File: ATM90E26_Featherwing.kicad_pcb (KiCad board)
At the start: 2 copper layers, 49.9 x 39.4 mm, 59 parts, among them J1 ST-PJ-312, J2 4P-SMD-2.0-90D, J3 4P-SMD-2.0-90D, J4 12V AC, Q1 8.192MHz, U1 ATM90E26, U2 CJT1117-5.0-SOT223

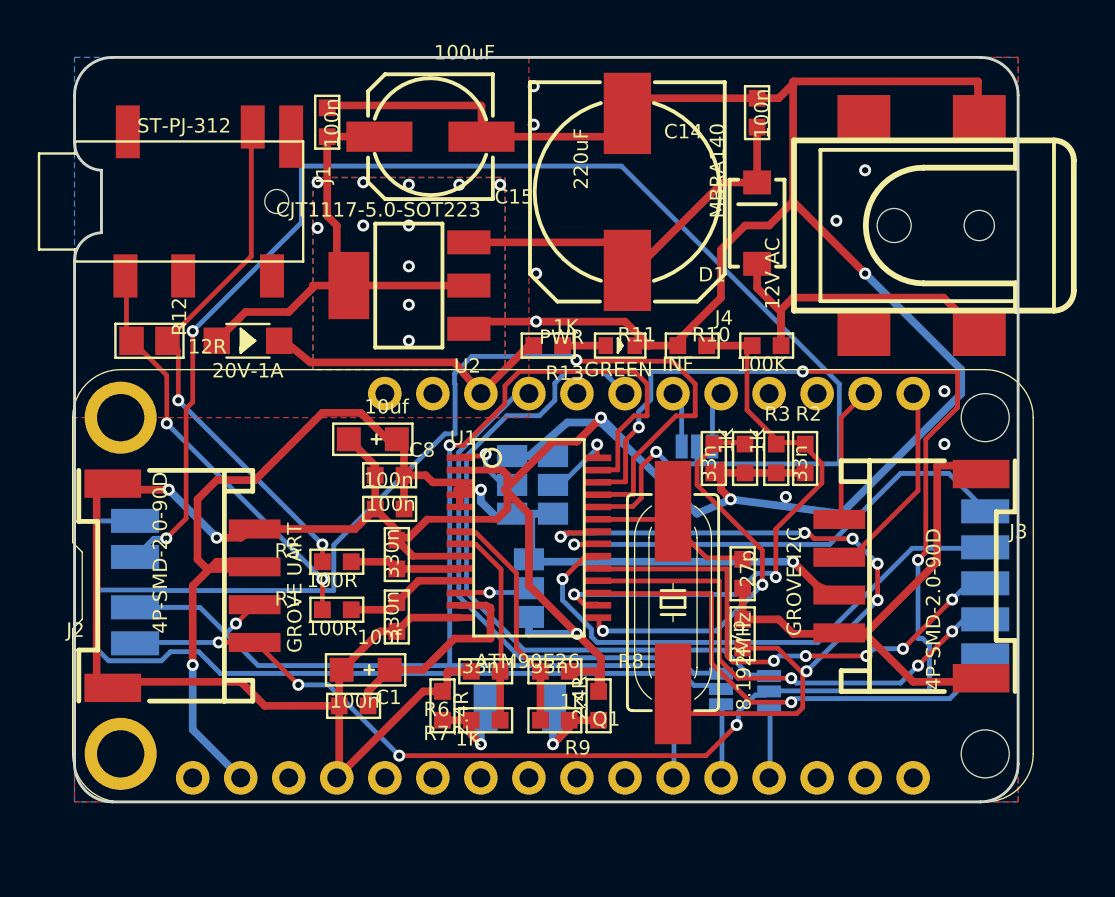
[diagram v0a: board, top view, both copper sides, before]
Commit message: Clean out tracks and zones, place parts
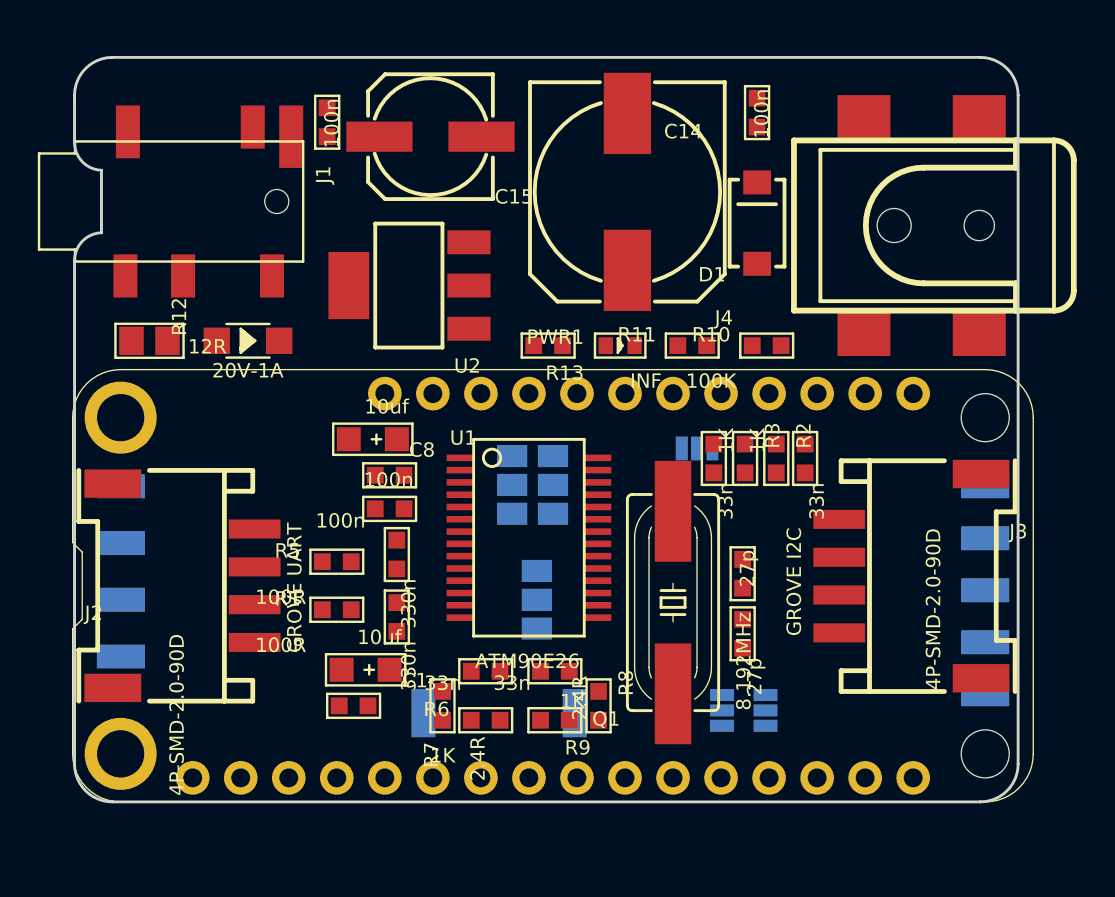
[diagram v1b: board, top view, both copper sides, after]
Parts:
- removed CS, I2N_IN, I2P_IN, INT, SCLK, SI/RX, SO/TX, WARN, ZX: WIREPADSMD1,27-254, SMD1,27-2,54
- removed CSMUX: JUMPER-PAD-3-NOYES_SILK, PAD-JUMPER-3-NO_YES_SILK
- removed PWR: GREEN, LED-0603
- removed the RXMUX at (157.7, 118.7)
- removed the SCKMUX at (155.2, 119.2)
- removed the TXMUX at (160.3, 118.8)
- removed USEL: JUMPER-PAD-3-NOFULL_BOX_SILK, PAD-JUMPER-3-NO_YES_SILK_FULL_BOX
- added CS1: WIREPADSMD1,27-254, ATM90E26_Featherwing:SMD1,27-2,54, B.Cu at (126.0, 108.0)
- added CSMUX1: JUMPER-PAD-3-NOYES_SILK, ATM90E26_Featherwing:PAD-JUMPER-3-NO_YES_SILK, B.Cu at (156.5, 106.0)
- added I2N_IN1: WIREPADSMD1,27-254, ATM90E26_Featherwing:SMD1,27-2,54, B.Cu at (142.0, 120.0)
- added I2P_IN1: WIREPADSMD1,27-254, ATM90E26_Featherwing:SMD1,27-2,54, B.Cu at (150.0, 120.0)
- added INT1: WIREPADSMD1,27-254, ATM90E26_Featherwing:SMD1,27-2,54, B.Cu at (171.7, 108.0)
- added PWR1: GREEN, ATM90E26_Featherwing:LED-0603, F.Cu at (152.4, 100.6)
- added RXMUX: JUMPER-PAD-3-NOYES_SILK, ATM90E26_Featherwing:PAD-JUMPER-3-NO_YES_SILK, B.Cu at (157.8, 119.8)
- added SCKMUX: JUMPER-PAD-2-NOYES_SILK, ATM90E26_Featherwing:PAD-JUMPER-2-NO_YES_SILK, B.Cu at (155.3, 120.3)
- added SCLK1: WIREPADSMD1,27-254, ATM90E26_Featherwing:SMD1,27-2,54, B.Cu at (126.0, 111.0)
- added SI/RX1: WIREPADSMD1,27-254, ATM90E26_Featherwing:SMD1,27-2,54, B.Cu at (126.0, 114.0)
- added SO/TX1: WIREPADSMD1,27-254, ATM90E26_Featherwing:SMD1,27-2,54, B.Cu at (126.0, 117.0)
- added TXMUX: JUMPER-PAD-3-NOYES_SILK, ATM90E26_Featherwing:PAD-JUMPER-3-NO_YES_SILK, B.Cu at (160.1, 119.8)
- added USEL1: JUMPER-PAD-3-NOFULL_BOX_SILK, ATM90E26_Featherwing:PAD-JUMPER-3-NO_YES_SILK_FULL_BOX, B.Cu at (148.0, 114.0)
- added WARN1: WIREPADSMD1,27-254, ATM90E26_Featherwing:SMD1,27-2,54, B.Cu at (171.7, 119.0)
- added ZX1: WIREPADSMD1,27-254, ATM90E26_Featherwing:SMD1,27-2,54, B.Cu at (171.7, 110.8)
- C1, C8: footprint AVX-A -> ATM90E26_Featherwing:AVX-A
- C10, C11, C12, C13, C16, C17, C2, C3, C4, C5, C6, C7, C9: footprint C0603 -> ATM90E26_Featherwing:C0603
- C14: footprint 140CLH-1010 -> ATM90E26_Featherwing:140CLH-1010
- C15: footprint 153CLV-0605 -> ATM90E26_Featherwing:153CLV-0605
- CF1, CF2: footprint SMD1,27-2,54 -> ATM90E26_Featherwing:SMD1,27-2,54
- D1: footprint SMA-DIODE -> ATM90E26_Featherwing:SMA-DIODE
- D2: footprint SOD-123 -> ATM90E26_Featherwing:SOD-123
- J1: footprint AUDIO6P-SMD-3.5-14.0X6.4X5.0MM -> ATM90E26_Featherwing:AUDIO6P-SMD-3.5-14.0X6.4X5.0MM
- J2, J3: footprint HW4-SMD-2.0-90D -> ATM90E26_Featherwing:HW4-SMD-2.0-90D
- J4: footprint DC_BARREL_JACK_SMD_2MM -> ATM90E26_Featherwing:DC_BARREL_JACK_SMD_2MM
- LOGO1: footprint OSHW-LOGO-M -> Symbols:OSHW-Logo2_7.3x6mm_SilkScreen
- MMD0, MMD1: footprint PAD-JUMPER-3-NO_YES_SILK_FULL_BOX -> ATM90E26_Featherwing:PAD-JUMPER-3-NO_YES_SILK_FULL_BOX
- MS1: footprint FEATHERWING_DIM -> ATM90E26_Featherwing:FEATHERWING_DIM
- Q1: footprint HC49UP -> ATM90E26_Featherwing:HC49UP
- R1, R10, R11, R13, R2, R3, R5, R6, R7, R8, R9: footprint R0603 -> ATM90E26_Featherwing:R0603
- R12: footprint 0805 -> ATM90E26_Featherwing:0805
- U1: footprint SSOP-28 -> ATM90E26_Featherwing:SSOP-28
- U2: footprint SOT-223 -> ATM90E26_Featherwing:SOT-223
- moved CF1 1.21 mm to (171.7, 116.2)
- moved CF2 0.37 mm to (171.7, 113.5)
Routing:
- net GND: track 261.6 -> 0.00 mm, vias 15 -> 0
- net /SCLK: track 90.9 -> 0.00 mm, vias 1 -> 0
- net /SO/TX: track 88.6 -> 0.00 mm, vias 7 -> 0
- net /CS: track 78.3 -> 0.00 mm, vias 3 -> 0
- net +3V3: track 68.5 -> 0.00 mm, vias 3 -> 0
- net /SI/RX: track 66.1 -> 0.00 mm, vias 2 -> 0
- net /CLKIN: track 40.7 -> 0.00 mm, vias 6 -> 0
- net /ATM_TX: track 36.3 -> 0.00 mm
- net /VP: track 31.2 -> 0.00 mm, vias 2 -> 0
- net Net-(INT1-Pad1): track 29.1 -> 0.00 mm, vias 1 -> 0
- net /I1N_IN: track 28.3 -> 0.00 mm, vias 2 -> 0
- net /ATM_RX: track 28.2 -> 0.00 mm
- net Net-(CF2-Pad1): track 27.0 -> 0.00 mm, vias 5 -> 0
- net Net-(CF1-Pad1): track 26.5 -> 0.00 mm, vias 3 -> 0
- net Net-(U1-Pad17): track 26.3 -> 0.00 mm, vias 1 -> 0
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- removed copper zone on B.Cu, net GND
- removed copper zone on F.Cu, net GND
- removed copper zone on B.Cu, net V_OUT
- removed copper zone on F.Cu, net V_OUT

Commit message: Initial autoroute
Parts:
- C7: footprint ATM90E26_Featherwing:C0603 -> C0603
- D2: footprint ATM90E26_Featherwing:SOD-123 -> SOD-123
- LOGO1: footprint Symbols:OSHW-Logo2_7.3x6mm_SilkScreen -> Symbols:OSHW-Logo2_7.3x6mm_Copper
- moved LOGO1 13.8 mm to (142.0, 97.5)
- renumbered RXMUX to RXMUX1, SCKMUX to SCKMUX1, TXMUX to TXMUX1
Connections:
- net Net-(C14-Pad+) renamed /AC_REC
- net Net-(C15-Pad+) renamed /5V_REG
- net Net-(D1-PadA) renamed /AC_VP
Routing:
- net GND: track 0.00 -> 236.2 mm, vias 0 -> 4
- net /SO/TX: track 0.00 -> 82.3 mm, vias 0 -> 4
- net +3V3: track 0.00 -> 67.8 mm, vias 0 -> 2
- net /SCLK: track 0.00 -> 61.3 mm, vias 0 -> 3
- net /SI/RX: track 0.00 -> 56.2 mm, vias 0 -> 4
- net /CS: track 0.00 -> 44.6 mm, vias 0 -> 1
- net /VP: track 0.00 -> 35.5 mm
- net Net-(U1-Pad17): track 0.00 -> 29.0 mm, vias 0 -> 1
- net /I1N_IN: track 0.00 -> 28.7 mm
- net /5V_REG: track 0.00 -> 27.9 mm, vias 0 -> 7
- net Net-(INT1-Pad1): track 0.00 -> 25.5 mm, vias 0 -> 1
- net Net-(CF1-Pad1): track 0.00 -> 23.7 mm, vias 0 -> 1
- net /ATM_RX: track 0.00 -> 23.3 mm, vias 0 -> 1
- net /I1P_IN: track 0.00 -> 23.1 mm
- net Net-(U1-Pad21): track 0.00 -> 22.5 mm, vias 0 -> 1
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- added copper zone on B.Cu, net /5V_REG
- added copper zone on F.Cu, net /5V_REG
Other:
- net class Default: clearance 0.1524 -> 0.15
- net class Power added: clearance 0.3, trace_width 0.4, via_dia 0.8, via_drill 0.4
- rule trace_clearance: 0.1524 -> 0.15
- board text added: "27/02/2018"
- board text added: "ATM90E26 Featherwing"
- board text added: "Tisham Dhar (@whatnick)"
- board text added: "v 1.3"
- board text removed: ">CNAME"
- board text removed: ">DESIGNER"
- board text removed: ">LAST_DATE_TIME"
- board text removed: ">VERSION"
- board text removed: ">WEBSITE"

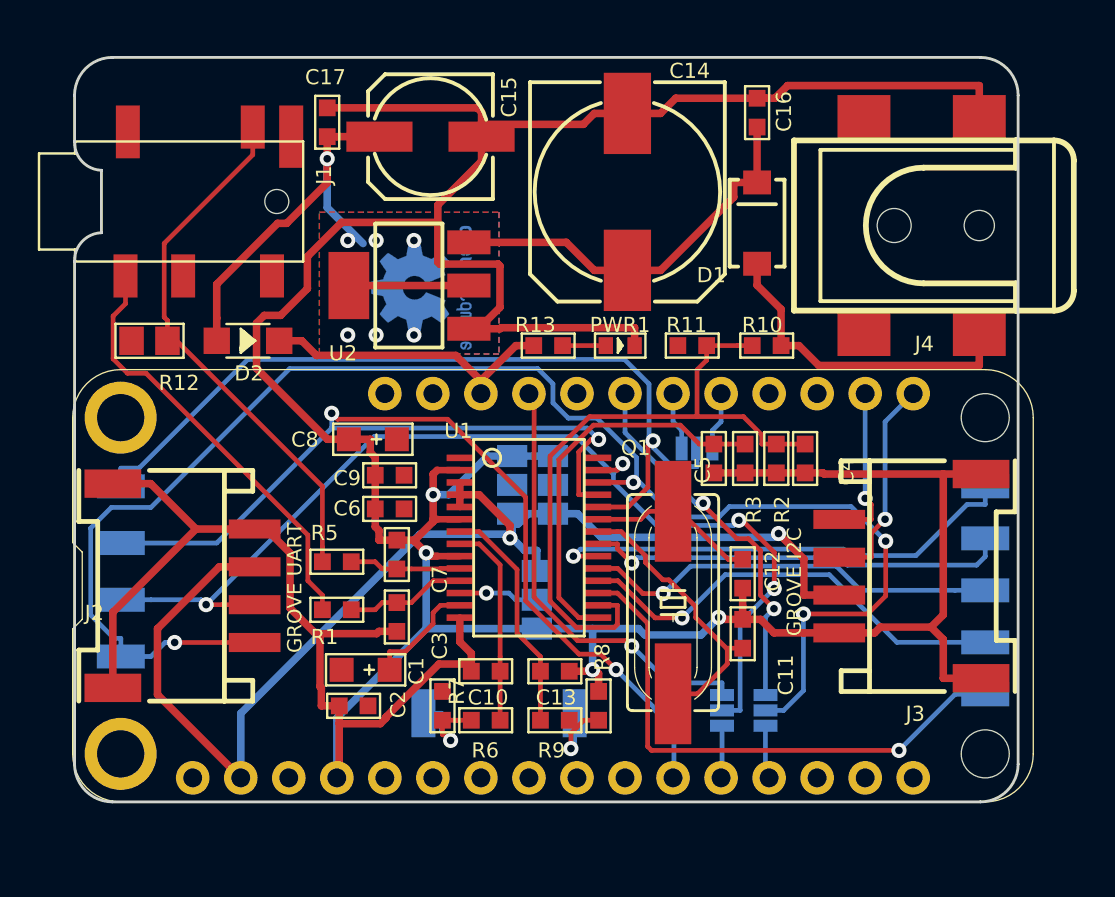
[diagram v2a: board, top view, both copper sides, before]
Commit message: Complete route and clean up silk
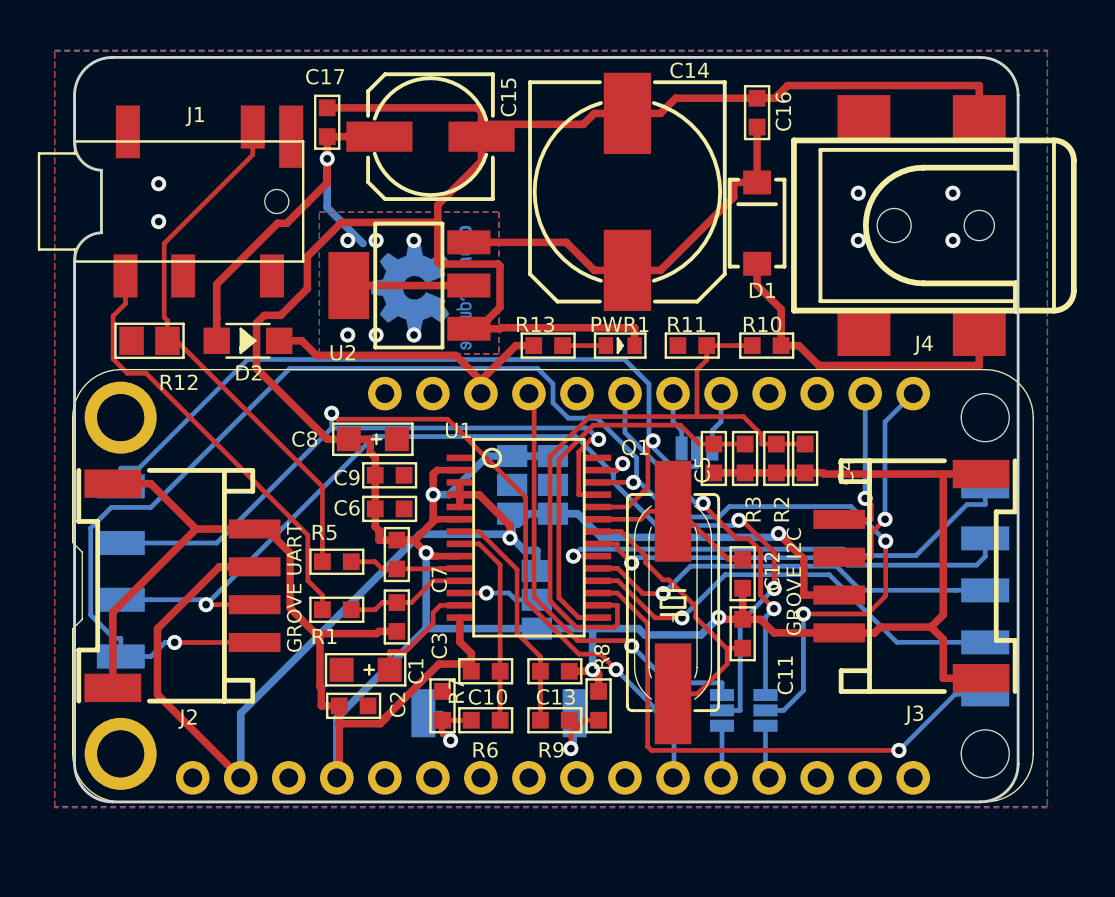
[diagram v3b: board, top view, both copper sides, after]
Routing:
- net GND: vias 4 -> 10
- added copper zone on B.Cu, net GND
- added copper zone on F.Cu, net GND
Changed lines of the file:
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@@
     (thickness 1.6)
     (drawings 20)
-    (tracks 526)
+    (tracks 532)
     (zones 0)
     (modules 59)
@@
   (page A4)
   (layers
-    (0 Top signal hide)
-    (31 Bottom signal hide)
+    (0 Top signal)
+    (31 Bottom signal)
     (32 B.Adhes user hide)
     (33 F.Adhes user hide)
@@
     (pad_to_mask_clearance 0.2)
     (aux_axis_origin 0 0)
-    (visible_elements 7FFFF9FF)
+    (visible_elements 7FFFFFFF)
     (pcbplotparams
       (layerselection 0x010fc_ffffffff)
@@
     (pad 14 smd rect (at 4.225 3.656 270) (size 0.348 1.397) (layers Top F.Paste F.Mask)
       (net 1 GND))
+    (model ${KISYS3DMOD}/Package_SO.3dshapes/SSOP-28_5.3x10.2mm_P0.65mm.step
+      (at (xyz 0 0 0))
+      (scale (xyz 1 1 1))
+      (rotate (xyz 0 0 -90))
+    )
   )
   (module ATM90E26_Featherwing:SOT-223 (layer Top)
@@
     (at 159.647 94.0816 90)
     (descr "<B>Diode</B><p>\nBasic SMA packaged diode. Good for reverse polarization protection. Common part #: MBRA140")
-    (fp_text reference D1 (at -2.286 -1.651) (layer F.SilkS)
+    (fp_text reference D1 (at -3.1184 1.053) (layer F.SilkS)
       (effects (font (size 0.8 0.8) (thickness 0.2)) (justify right top))
     )
@@
   (module ATM90E26_Featherwing:HW4-SMD-2.0-90D (layer Top)
     (at 132.977 113.259 90)
-    (fp_text reference J2 (at -1.905 -8.89 -180) (layer F.SilkS)
+    (fp_text reference J2 (at -7.441 -3.877 -180) (layer F.SilkS)
       (effects (font (size 0.8 0.8) (thickness 0.2)) (justify left bottom))
     )
@@
     (pad "" np_thru_hole circle (at 0 -2.275 90) (size 1.8 1.8) (drill 1.8) (layers *.Cu))
     (pad "" np_thru_hole circle (at 0 2.225 90) (size 1.6 1.6) (drill 1.6) (layers *.Cu))
+    (model ${KIPRJMOD}/3dmodels/CUI_PJ-002BH-SMT-TR.step
+      (offset (xyz 0 -7.5 0))
+      (scale (xyz 1 1 1))
+      (rotate (xyz 90 180 180))
+    )
   )
   (module ATM90E26_Featherwing:AVX-A (layer Top)
@@
   (module ATM90E26_Featherwing:AUDIO6P-SMD-3.5-14.0X6.4X5.0MM (layer Top)
     (at 121.674 92.9386 180)
-    (fp_text reference J1 (at -14.605 1.905 90) (layer F.SilkS)
+    (fp_text reference J1 (at -8.826 5.0386 180) (layer F.SilkS)
       (effects (font (size 0.8 0.8) (thickness 0.2)) (justify right top))
     )
@@
   (gr_line (start 124.975524 94.5896) (end 124.975524 91.2876) (layer Edge.Cuts) (width 0.15))
   (gr_arc (start 125.025524 89.8136) (end 124.975524 91.2876) (angle 90) (layer Edge.Cuts) (width 0.15))
+  (via (at 128 94) (size 0.8) (drill 0.4) (layers Top Bottom) (net 1))
+  (via (at 128 92) (size 0.8) (drill 0.4) (layers Top Bottom) (net 1))
+  (via (at 170 95) (size 0.8) (drill 0.4) (layers Top Bottom) (net 1))
+  (via (at 170 92.5) (size 0.8) (drill 0.4) (layers Top Bottom) (net 1))
+  (via (at 165 95) (size 0.8) (drill 0.4) (layers Top Bottom) (net 1))
+  (via (at 165 92.5) (size 0.8) (drill 0.4) (layers Top Bottom) (net 1))
   (segment (start 144.915 99.6696) (end 146.050001 98.534599) (width 0.4) (layer Top) (net 1))
   (segment (start 146.050001 98.534599) (end 146.050001 96.348599) (width 0.4) (layer Top) (net 1))
@@
   )
   (zone (net 70) (net_name /5V_REG) (layer Top) (hatch edge 0.508)
+    (priority 1)
     (connect_pads (clearance 0.508))
     (min_thickness 0.254)
@@
   )
   (zone (net 70) (net_name /5V_REG) (layer Bottom) (hatch edge 0.508)
+    (priority 1)
     (connect_pads (clearance 0.508))
     (min_thickness 0.254)
@@
       )
     )
+  )
+  (zone (net 1) (net_name GND) (layer Top) (hatch edge 0.508)
+    (connect_pads (clearance 0.508))
+    (min_thickness 0.254)
+    (fill yes (arc_segments 16) (thermal_gap 0.508) (thermal_bridge_width 0.508))
+    (polygon
+      (pts
+        (xy 122.5 85) (xy 175 85) (xy 175 125) (xy 122.5 125)
+      )
+    )
+  )
+  (zone (net 1) (net_name GND) (layer Bottom) (hatch edge 0.508)
+    (connect_pads (clearance 0.508))
+    (min_thickness 0.254)
+    (fill yes (arc_segments 16) (thermal_gap 0.508) (thermal_bridge_width 0.508))
+    (polygon
+      (pts
+        (xy 122.5 84.940731) (xy 175 84.940731) (xy 175 124.940731) (xy 122.5 124.940731)
+      )
+    )
